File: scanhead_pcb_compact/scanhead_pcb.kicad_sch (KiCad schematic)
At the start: 28 parts, among them J1 Screw_Terminal_01x04, J2 FPC 15 pin molex vertical, J3 FPC molex 4 pin, J6 jumper wire 2 pin, J7 jumper wire 2 pin, Q1 IRFML8244, U1 DIGIPOT_50K, U2 U_IC-HKB, U3 STSPIN230

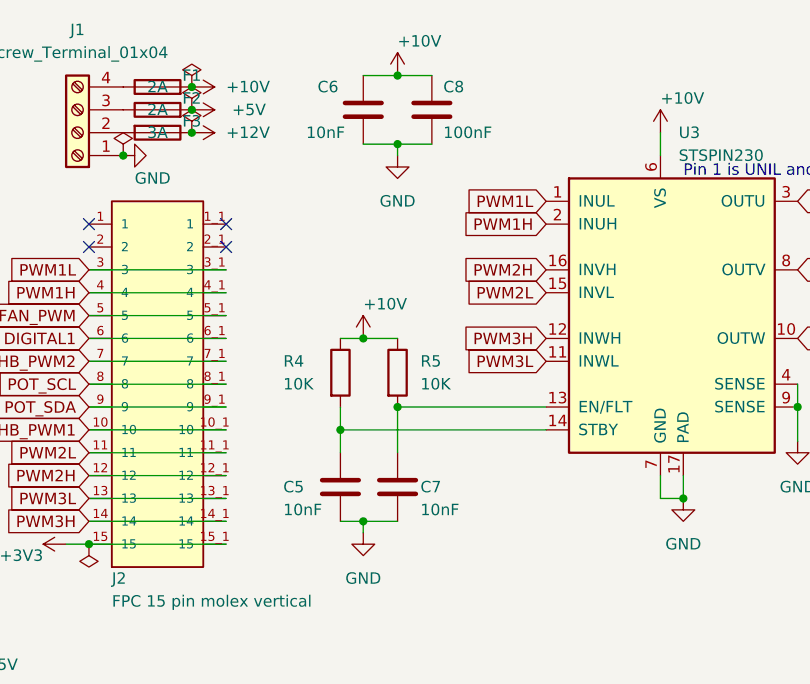
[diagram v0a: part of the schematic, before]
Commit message: updated compact scanhead
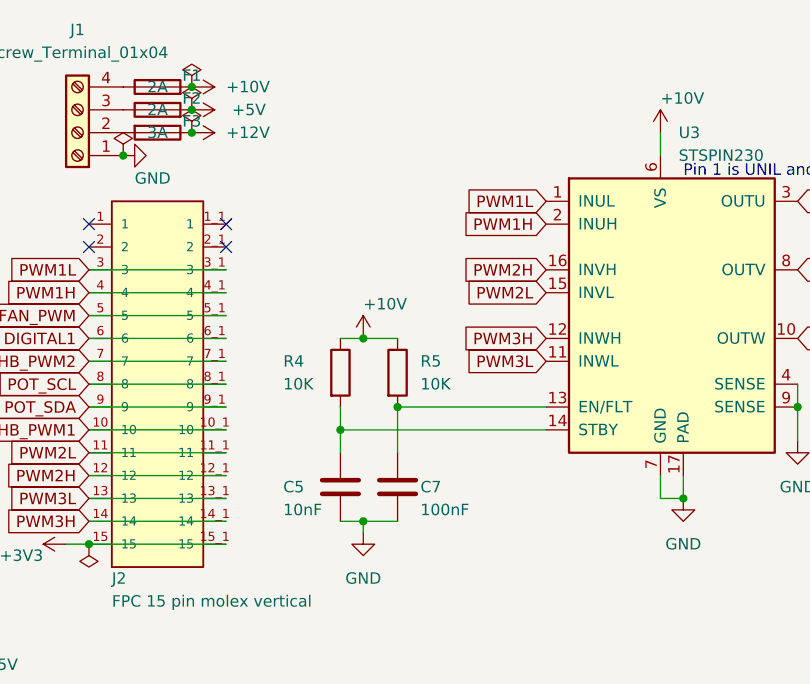
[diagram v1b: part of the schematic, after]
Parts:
- removed C6: 10nF, Capacitor_SMD:C_0805_2012Metric_Pad1.15x1.40mm_HandSolder, symbol Device:C
- removed C8: 100nF, Capacitor_SMD:C_0805_2012Metric_Pad1.15x1.40mm_HandSolder, symbol Device:C
- C1, C2, C3, C4, C5: footprint Capacitor_SMD:C_0805_2012Metric_Pad1.15x1.40mm_HandSolder -> Capacitor_SMD:C_0805_2012Metric_Pad1.18x1.45mm_HandSolder
- C7: value 10nF -> 100nF; footprint Capacitor_SMD:C_0805_2012Metric_Pad1.15x1.40mm_HandSolder -> Capacitor_SMD:C_0805_2012Metric_Pad1.18x1.45mm_HandSolder
- J1: footprint (none) -> Connector_Molex:Molex_KK-254_AE-6410-04A_1x04_P2.54mm_Vertical
- R1, R2, R3, R4, R5: footprint Resistor_SMD:R_0805_2012Metric_Pad1.15x1.40mm_HandSolder -> Resistor_SMD:R_0805_2012Metric_Pad1.20x1.40mm_HandSolder

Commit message: updated model
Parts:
- removed H1, H2: MountingHole, MountingHole:MountingHole_3.2mm_M3, symbol Mechanical:MountingHole
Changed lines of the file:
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@@
     (pin "1")
-  )
-  (symbol (lib_id "Mechanical:MountingHole") (at 187.96 34.29 0) (unit 1)
-    (in_bom yes) (on_board yes)
-    (property "Reference" "H2" (id 0) (at 190.5 33.1216 0)
-      (effects (font (size 1.27 1.27)) (justify left))
-    )
-    (property "Value" "MountingHole" (id 1) (at 190.5 35.433 0)
-      (effects (font (size 1.27 1.27)) (justify left))
-    )
-    (property "Footprint" "MountingHole:MountingHole_3.2mm_M3" (id 2) (at 187.96 34.29 0)
-      (effects (font (size 1.27 1.27)) hide)
-    )
-    (property "Datasheet" "~" (id 3) (at 187.96 34.29 0)
-      (effects (font (size 1.27 1.27)) hide)
-    )
-  )
-  (symbol (lib_id "Mechanical:MountingHole") (at 187.96 24.13 0) (unit 1)
-    (in_bom yes) (on_board yes)
-    (property "Reference" "H1" (id 0) (at 190.5 22.9616 0)
-      (effects (font (size 1.27 1.27)) (justify left))
-    )
-    (property "Value" "MountingHole" (id 1) (at 190.5 25.273 0)
-      (effects (font (size 1.27 1.27)) (justify left))
-    )
-    (property "Footprint" "MountingHole:MountingHole_3.2mm_M3" (id 2) (at 187.96 24.13 0)
-      (effects (font (size 1.27 1.27)) hide)
-    )
-    (property "Datasheet" "~" (id 3) (at 187.96 24.13 0)
-      (effects (font (size 1.27 1.27)) hide)
-    )
   )
   (symbol (lib_id "Connector_Generic:Conn_01x04") (at 158.75 54.61 180) (unit 1)
@@
       (reference "F3") (unit 1) (value "3A") (footprint "Fuse:Fuse_1206_3216Metric")
     )
-    (path "/00000000-0000-0000-0000-00005ff46d80"
-      (reference "H1") (unit 1) (value "MountingHole") (footprint "MountingHole:MountingHole_3.2mm_M3")
-    )
-    (path "/00000000-0000-0000-0000-00005ff4680b"
-      (reference "H2") (unit 1) (value "MountingHole") (footprint "MountingHole:MountingHole_3.2mm_M3")
-    )
     (path "/33573c6f-38bc-4f07-8547-bd249295dde8"

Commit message: updated boards
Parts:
- removed D1: 50V_1A, Diode_SMD:D_SMA_Handsoldering, symbol Device:D_Schottky
- removed J3: FPC molex 4 pin, sockets_scanhead:Molex_200528-0040_1x04-1MP_P1.00mm_Horizontal, symbol Connector_Generic:Conn_01x04
- removed J7: jumper wire 2 pin, Connector_Molex:Molex_KK-254_AE-6410-02A_1x02_P2.54mm_Vertical, symbol Connector_Generic:Conn_01x02
- removed Q1: IRFML8244, Package_TO_SOT_SMD:SOT-23, symbol Transistor_FET:IRLB8721PBF
- added C6: 220pF, Capacitor_SMD:C_0805_2012Metric_Pad1.18x1.45mm_HandSolder, symbol Device:C
- added C8: 1uF, Capacitor_SMD:C_0805_2012Metric_Pad1.18x1.45mm_HandSolder, symbol Device:C
- added J3: Conn_01x02, Connector_PinHeader_2.54mm:PinHeader_1x02_P2.54mm_Vertical, symbol Connector_Generic:Conn_01x02
- added R10, R7: 22K, Resistor_SMD:R_0805_2012Metric_Pad1.20x1.40mm_HandSolder, symbol Device:R
- added R11: 1K5, Resistor_SMD:R_0805_2012Metric_Pad1.20x1.40mm_HandSolder, symbol Device:R
- added R12, R6, R8, R9: 8K2, Resistor_SMD:R_0805_2012Metric_Pad1.20x1.40mm_HandSolder, symbol Device:R
- added TP2: HSync, TestPoint:TestPoint_Pad_D1.0mm, symbol Connector:TestPoint
- added U4, U5: MIC920, Package_TO_SOT_SMD:SOT-353_SC-70-5_Handsoldering, symbol photodiode-cape:MIC920
- R1: value 10K -> 22K
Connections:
- net +5V: now also R1.2, C8.1, R8.2, U4.5 (V+), U5.5 (V+)
- net FAN_PWM: no longer R1.1
- net GND: now also C8.2, J3.1 (Pin_1), R12.2, R6.1, R9.1, U4.2 (V-), U5.2 (V-); no longer R1.2
- new net: R1.1, R6.2, U4.1 (+)
- new net: C6.2, J3.2 (Pin_2), R7.1, U4.3 (-)
- new net: R10.2, R8.1, R9.2, U5.1 (+)
- new net: R10.1, R11.2, TP2.1, U5.4
- new net ANALOG: C6.1, R7.2, U4.4, U5.3 (-)
- new net DIGITAL: R11.1, R12.1
- no-connect marks 5 -> 4
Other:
- note added: "Photo Diode Amp"
- note added: "Schmitt Trigger"
- note removed: "fan"
- note removed: "photodiode_digi"
- moved on the sheet: C1, C2, C3, C4, C5, C7, F1, F2, F3, J1, J2, J6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

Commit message: routed new boards for compact scanhead
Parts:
- added C9: 10nF, Capacitor_SMD:C_0805_2012Metric_Pad1.18x1.45mm_HandSolder, symbol Device:C
- added R13, R14, R15: 10K, Resistor_SMD:R_0805_2012Metric_Pad1.20x1.40mm_HandSolder, symbol Device:R
- added U6, U7, U8: DRV5033FAxDBZ, Package_TO_SOT_SMD:SOT-23, symbol Sensor_Magnetic:DRV5033FAxDBZ
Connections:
- net DIGITAL1 is gone; now on net POT_SCL: J2.6, J2.6_1 (6)
- net FAN_PWM is gone; now on net POT_SDA: J2.5, J2.5_1 (5)
- net +3V3: now also C9.1, R13.1, R14.1, R15.1, U6.1 (VCC), U7.1 (VCC), U8.1 (VCC)
- net DIGITAL: now also J2.14, J2.14_1 (14)
- net GND: now also C9.2, U6.3 (GND), U7.3 (GND), U8.3 (GND)
- net IC_HB_PWM1: now also J2.7, J2.7_1 (7); no longer J2.10, J2.10_1 (10)
- net IC_HB_PWM2: now also J2.8, J2.8_1 (8); no longer J2.7, J2.7_1 (7)
- net POT_SCL: no longer J2.8, J2.8_1 (8)
- net POT_SDA: no longer J2.9, J2.9_1 (9)
- net PWM2H: now also J2.2, J2.2_1 (2); no longer J2.12, J2.12_1 (12)
- net PWM2L: now also J2.1, J2.1_1 (1); no longer J2.11, J2.11_1 (11)
- net PWM3H: now also J2.10, J2.10_1 (10); no longer J2.14, J2.14_1 (14)
- net PWM3L: now also J2.9, J2.9_1 (9); no longer J2.13, J2.13_1 (13)
- new net HALL1: J2.11, J2.11_1 (11), R15.2, U8.2 (OUT)
- new net HALL2: J2.12, J2.12_1 (12), R13.2, U6.2 (OUT)
- new net HALL3: J2.13, J2.13_1 (13), R14.2, U7.2 (OUT)
- no-connect marks 4 -> 0
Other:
- moved on the sheet: C8

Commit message: added design of june
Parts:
- added R16, R17, R18: Zero, Resistor_SMD:R_0805_2012Metric_Pad1.20x1.40mm_HandSolder, symbol Device:R
- added R19: R, Resistor_SMD:R_2512_6332Metric_Pad1.40x3.35mm_HandSolder, symbol Device:R
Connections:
- net +10V: now also R19.2; no longer F1.2, R4.1, R5.1
- net +5V: now also R4.1, R5.1
- net IC_HB_PWM2: now also J2.6, J2.6_1 (6); no longer J2.8, J2.8_1 (8)
- net PH1: now also R16.2, R17.2, R18.2; no longer U3.10 (OUTW), U3.3 (OUTU), U3.8 (OUTV)
- net POT_SCL: now also J2.8, J2.8_1 (8); no longer J2.6, J2.6_1 (6)
- net POT_SDA: now also J2.9, J2.9_1 (9); no longer J2.5, J2.5_1 (5)
- net PWM3L: now also J2.5, J2.5_1 (5); no longer J2.9, J2.9_1 (9)
- new net: F1.2, R19.1
- new net: R18.1, U3.10 (OUTW)
- new net: R16.1, U3.3 (OUTU)
- new net: R17.1, U3.8 (OUTV)
